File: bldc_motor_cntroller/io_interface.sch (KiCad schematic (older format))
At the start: 29 parts, among them J1 SM06B-SRSS-TB, J2 Conn_01x18, J5 0475900001, J6 TC2030 Tag-connect, J7 SH-SM02B-SRSS, SW1 SW_Push, SW2 SW_Push, U1 TCAN332GDCNT

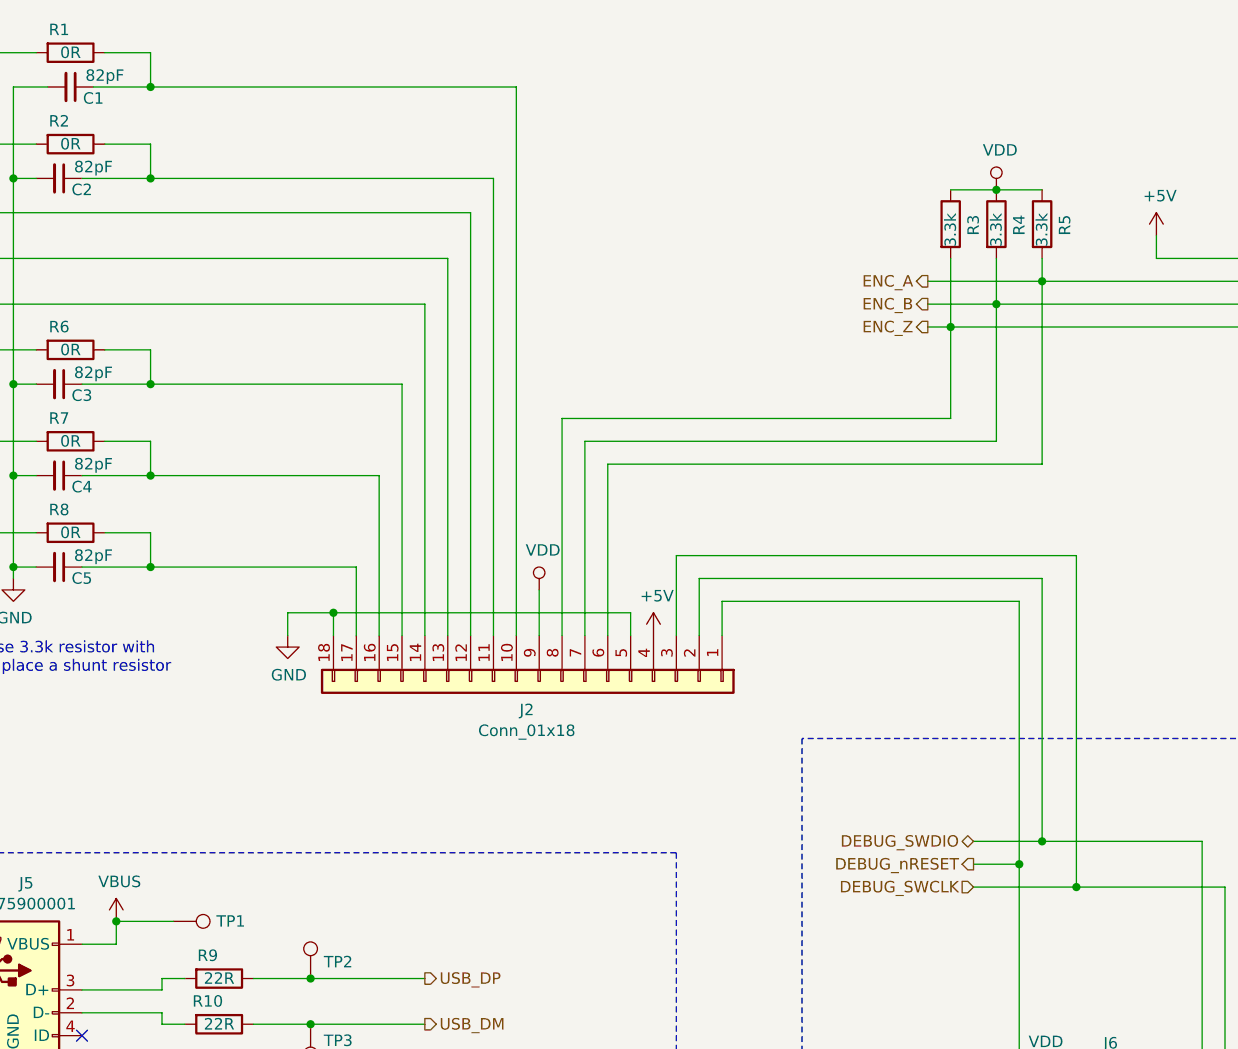
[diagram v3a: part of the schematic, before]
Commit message: swapped connections for better routing. highlighted serial gpios.
Signed-off-by: azmat bilal <azmat.bilal@outlook.com>
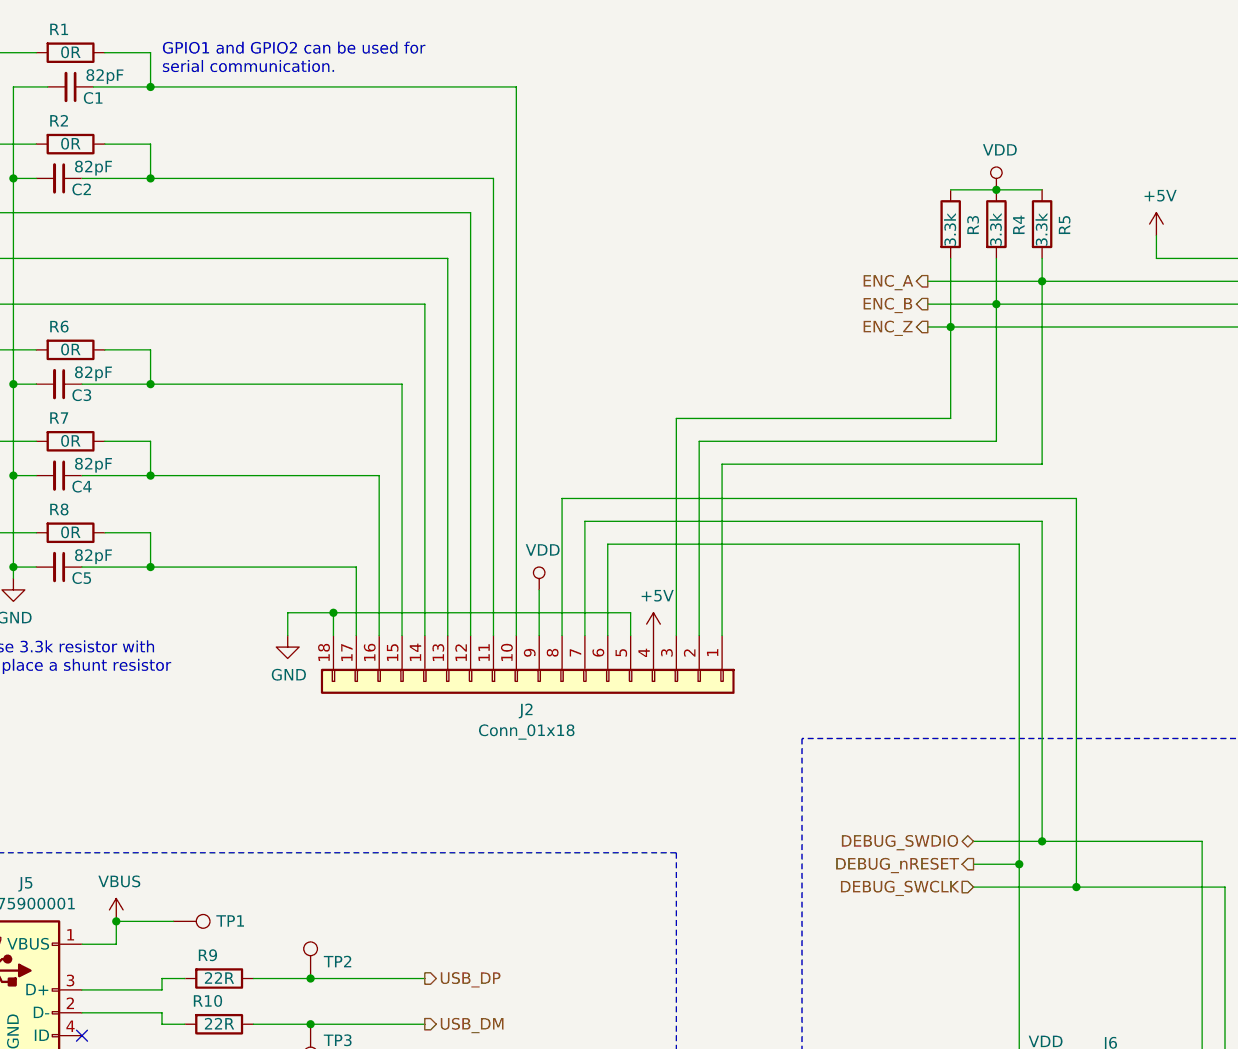
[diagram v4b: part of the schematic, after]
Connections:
- net DEBUG_SWCLK: now also J2.8 (Pin_8); no longer J2.3 (Pin_3)
- net DEBUG_SWDIO: now also J2.7 (Pin_7); no longer J2.2 (Pin_2)
- net DEBUG_nRESET: now also J2.6 (Pin_6); no longer J2.1 (Pin_1)
- net ENC_A: now also J2.1 (Pin_1); no longer J2.6 (Pin_6)
- net ENC_B: now also J2.2 (Pin_2); no longer J2.7 (Pin_7)
- net ENC_Z: now also J2.3 (Pin_3); no longer J2.8 (Pin_8)
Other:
- note added: "GPIO1 and GPIO2 can be used for\nserial communication."
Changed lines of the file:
@@
 	6300 2200 6300 2600
 Wire Wire Line
-	6300 2600 4600 2600
-Wire Wire Line
-	4600 2600 4600 3550
+	6300 2600 5100 2600
 Wire Wire Line
 	6500 2100 6500 2700
 Wire Wire Line
-	6500 2700 4700 2700
-Wire Wire Line
-	4700 2700 4700 3550
+	6500 2700 5200 2700
 Wire Wire Line
 	6700 2000 6700 2800
 Wire Wire Line
-	6700 2800 4800 2800
-Wire Wire Line
-	4800 2800 4800 3550
+	6700 2800 5300 2800
 $Comp
 L power:+5V #PWR?
@@
 Wire Wire Line
 	6600 5650 6750 5650
-Wire Wire Line
-	6600 4550 6600 3400
-Wire Wire Line
-	6600 3400 5300 3400
-Wire Wire Line
-	5300 3400 5300 3550
 Connection ~ 6600 4550
-Wire Wire Line
-	6700 4450 6700 3300
-Wire Wire Line
-	6700 3300 5200 3300
-Wire Wire Line
-	5200 3300 5200 3550
 Connection ~ 6700 4450
 Wire Wire Line
 	6700 4450 7400 4450
-Wire Wire Line
-	6850 4650 6850 3200
-Wire Wire Line
-	6850 3200 5100 3200
-Wire Wire Line
-	5100 3200 5100 3550
 Connection ~ 6850 4650
 Wire Wire Line
@@
 Wire Wire Line
 	4500 3350 4500 3550
+Wire Wire Line
+	6600 3150 4800 3150
+Wire Wire Line
+	4800 3150 4800 3550
+Wire Wire Line
+	6600 3150 6600 4550
+Wire Wire Line
+	6700 3050 4700 3050
+Wire Wire Line
+	4700 3050 4700 3550
+Wire Wire Line
+	6700 3050 6700 4450
+Wire Wire Line
+	6850 2950 4600 2950
+Wire Wire Line
+	4600 2950 4600 3550
+Wire Wire Line
+	6850 2950 6850 4650
+Wire Wire Line
+	5300 3550 5300 2800
+Wire Wire Line
+	5200 3550 5200 2700
+Wire Wire Line
+	5100 3550 5100 2600
+Text Notes 2850 1100 0    50   ~ 0
+GPIO1 and GPIO2 can be used for\nserial communication.
 $EndSCHEMATC

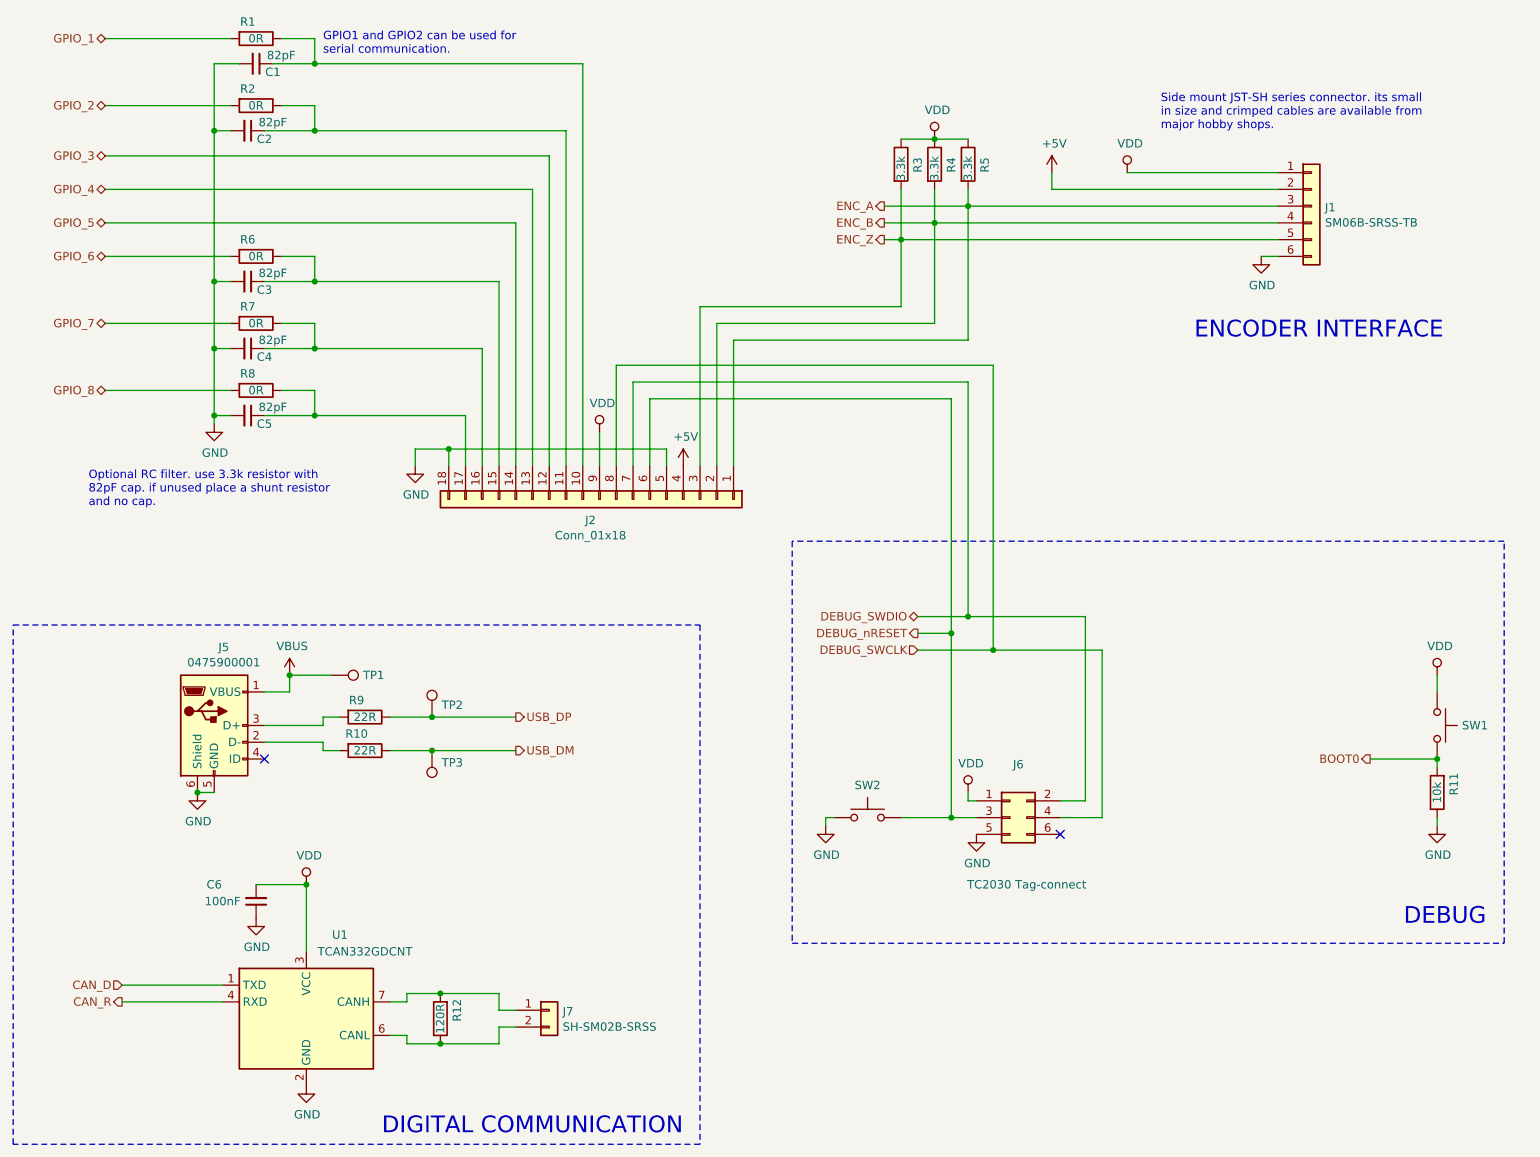
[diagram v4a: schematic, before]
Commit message: changed the SMD connector to JST SH (from JST SHL)
Signed-off-by: azmat bilal <azmat.bilal@outlook.com>
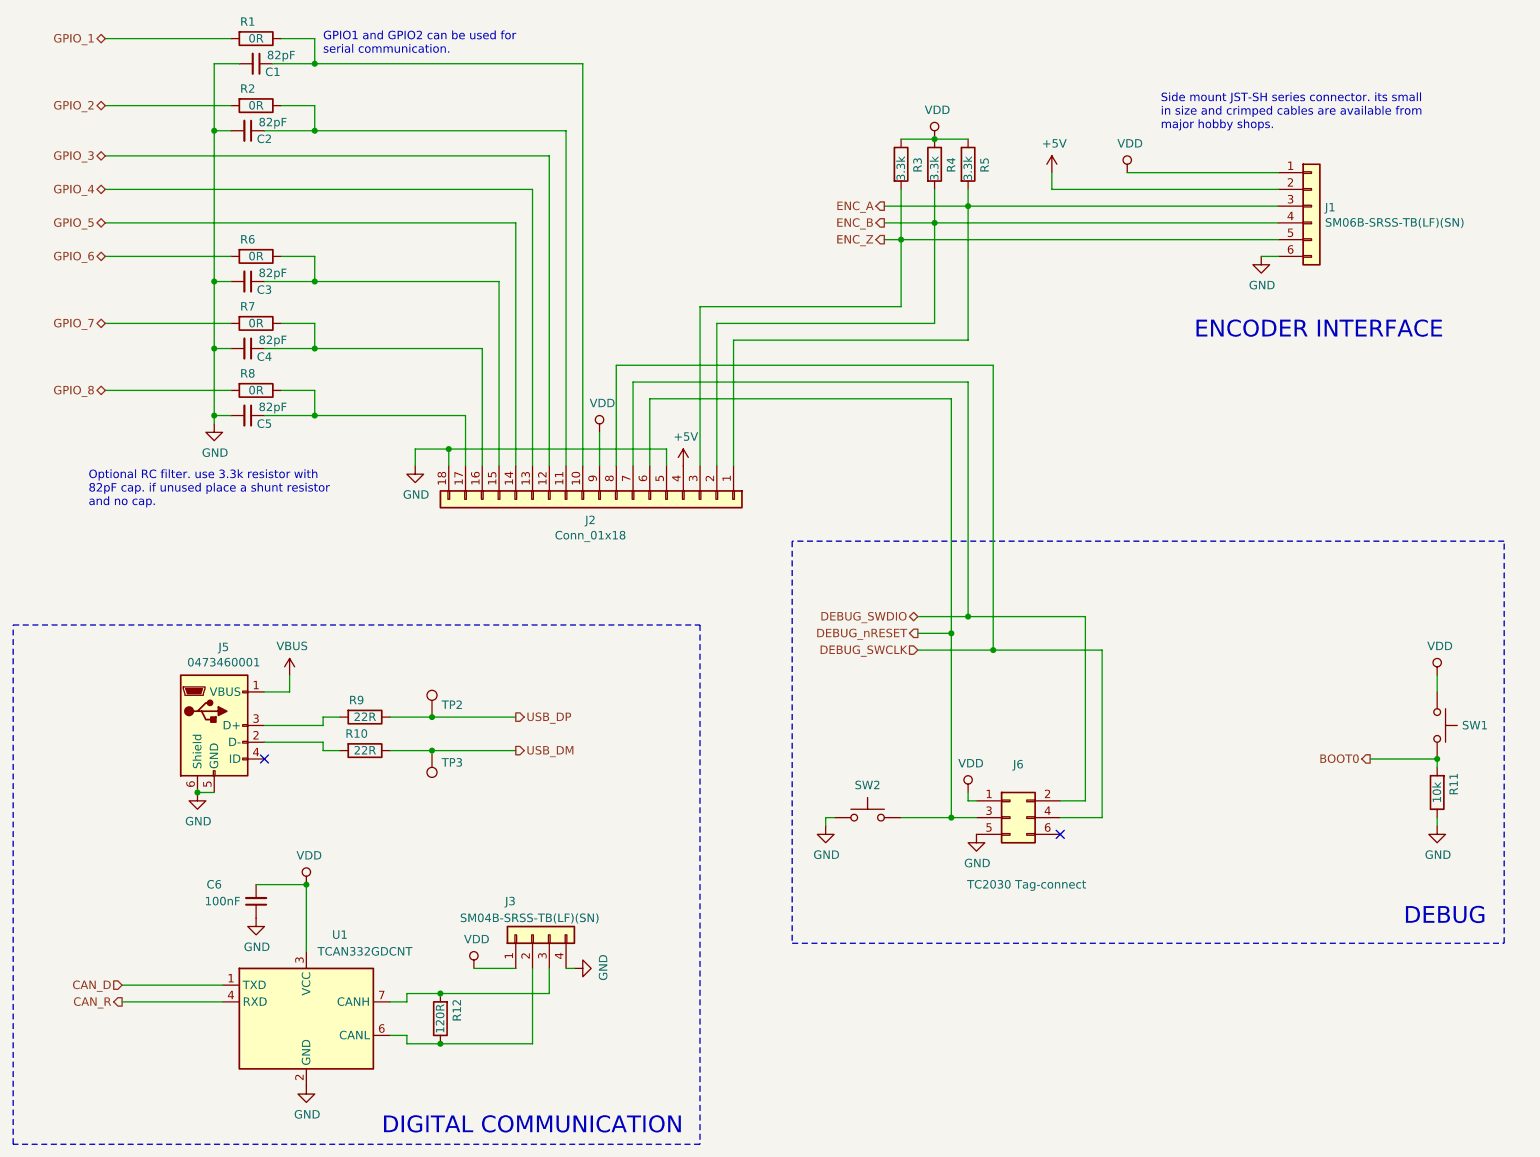
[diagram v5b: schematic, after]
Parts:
- removed J7: SH-SM02B-SRSS, Connector_JST:JST_SH_SM02B-SRSS-TB_1x02-1MP_P1.00mm_Horizontal, symbol Connector_Generic:Conn_01x02
- removed TP1: TestPoint, TestPoint:TestPoint_Pad_D1.5mm, symbol Connector:TestPoint
- added J3: SM04B-SRSS-TB(LF)(SN), Connector_JST:JST_SH_SM04B-SRSS-TB_1x04-1MP_P1.00mm_Horizontal, symbol Connector_Generic:Conn_01x04
- J1: value SM06B-SRSS-TB -> SM06B-SRSS-TB(LF)(SN)
- J5: value 0475900001 -> 0473460001; footprint Connector_USB:USB_Micro-AB_Molex_47590-0001 -> Connector_USB:USB_Micro-B_Molex_47346-0001
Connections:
- net GND: now also J3.4 (Pin_4)
- net VDD: now also J3.1 (Pin_1)
- net at R12.1, U1.6 (CANL): now also J3.2 (Pin_2)
- net at R12.2, U1.7 (CANH): now also J3.3 (Pin_3)
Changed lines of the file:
@@
 P 2200 5100
 F 0 "J5" H 2257 5567 50  0000 C CNN
-F 1 "0475900001" H 2257 5476 50  0000 C CNN
-F 2 "Connector_USB:USB_Micro-AB_Molex_47590-0001" H 2350 5050 50  0001 C CNN
+F 1 "0473460001" H 2257 5476 50  0000 C CNN
+F 2 "Connector_USB:USB_Micro-B_Molex_47346-0001" H 2350 5050 50  0001 C CNN
 F 3 "~" H 2350 5050 50  0001 C CNN
 	1    2200 5100
@@
 	2650 4900 2500 4900
 $Comp
-L Connector:TestPoint TP1
-U 1 1 5E39A600
-P 2900 4800
-F 0 "TP1" V 2900 4988 50  0000 L CNN
-F 1 "TestPoint" V 2945 4988 50  0001 L CNN
-F 2 "TestPoint:TestPoint_Pad_D1.5mm" H 3100 4800 50  0001 C CNN
-F 3 "~" H 3100 4800 50  0001 C CNN
-	1    2900 4800
-	0    1    1    0
-$EndComp
-Wire Wire Line
-	2900 4800 2650 4800
-Connection ~ 2650 4800
-$Comp
 L Connector:TestPoint TP2
 U 1 1 5E39DE72
@@
 Wire Wire Line
 	2750 6050 2750 6450
-$Comp
-L Connector_Generic:Conn_01x02 J7
-U 1 1 5E3CD122
-P 4200 6800
-F 0 "J7" H 4280 6792 50  0000 L CNN
-F 1 "SH-SM02B-SRSS" H 4280 6701 50  0000 L CNN
-F 2 "Connector_JST:JST_SH_SM02B-SRSS-TB_1x02-1MP_P1.00mm_Horizontal" H 4200 6800 50  0001 C CNN
-F 3 "~" H 4200 6800 50  0001 C CNN
-	1    4200 6800
-	1    0    0    -1
-$EndComp
-$Comp
-L Device:R R12
-U 1 1 5E3D290A
-P 3550 6850
-F 0 "R12" V 3450 6800 50  0000 C CNN
-F 1 "120R" V 3550 6850 50  0000 C CNN
-F 2 "Resistor_SMD:R_0402_1005Metric" V 3480 6850 50  0001 C CNN
-F 3 "~" H 3550 6850 50  0001 C CNN
-	1    3550 6850
-	-1   0    0    1
-$EndComp
 Wire Wire Line
 	3250 6750 3350 6750
@@
 	3350 6700 3550 6700
 Wire Wire Line
-	3900 6700 3900 6800
-Wire Wire Line
-	3900 6800 4000 6800
-Connection ~ 3550 6700
-Wire Wire Line
-	3550 6700 3900 6700
-Wire Wire Line
 	3250 6950 3350 6950
 Wire Wire Line
@@
 Wire Wire Line
 	3350 7000 3550 7000
-Wire Wire Line
-	3900 7000 3900 6900
-Wire Wire Line
-	3900 6900 4000 6900
-Connection ~ 3550 7000
-Wire Wire Line
-	3550 7000 3900 7000
 Text HLabel 1650 6650 0    50   Input ~ 0
 CAN_D
@@
 AR Path="/5E2D92A8/5E38F4AB" Ref="J1"  Part="1"
 F 0 "J1" H 8830 1992 50  0000 L CNN
-F 1 "SM06B-SRSS-TB" H 8830 1901 50  0000 L CNN
+F 1 "SM06B-SRSS-TB(LF)(SN)" H 8830 1901 50  0000 L CNN
 F 2 "Connector_JST:JST_SH_SM06B-SRSS-TB_1x06-1MP_P1.00mm_Horizontal" H 8750 2000 50  0001 C CNN
 F 3 "~" H 8750 2000 50  0001 C CNN
@@
 Text Notes 2850 1100 0    50   ~ 0
 GPIO1 and GPIO2 can be used for\nserial communication.
+$Comp
+L Connector_Generic:Conn_01x04 J3
+U 1 1 5E58BAE0
+P 4100 6350
+F 0 "J3" V 4300 6450 50  0000 L CNN
+F 1 "SM04B-SRSS-TB(LF)(SN)" V 4200 5950 50  0000 L CNN
+F 2 "Connector_JST:JST_SH_SM04B-SRSS-TB_1x04-1MP_P1.00mm_Horizontal" H 4100 6350 50  0001 C CNN
+F 3 "~" H 4100 6350 50  0001 C CNN
+	1    4100 6350
+	0    -1   -1   0
+$EndComp
+$Comp
+L power:VDD #PWR02
+U 1 1 5E58D69E
+P 3750 6550
+F 0 "#PWR02" H 3750 6400 50  0001 C CNN
+F 1 "VDD" H 3767 6723 50  0000 C CNN
+F 2 "" H 3750 6550 50  0001 C CNN
+F 3 "" H 3750 6550 50  0001 C CNN
+	1    3750 6550
+	1    0    0    -1
+$EndComp
+$Comp
+L power:GND #PWR03
+U 1 1 5E58D909
+P 4350 6550
+F 0 "#PWR03" H 4350 6300 50  0001 C CNN
+F 1 "GND" H 4355 6377 50  0000 C CNN
+F 2 "" H 4350 6550 50  0001 C CNN
+F 3 "" H 4350 6550 50  0001 C CNN
+	1    4350 6550
+	0    -1   -1   0
+$EndComp
+Wire Wire Line
+	4350 6550 4300 6550
+$Comp
+L Device:R R12
+U 1 1 5E3D290A
+P 3550 6850
+F 0 "R12" V 3450 6800 50  0000 C CNN
+F 1 "120R" V 3550 6850 50  0000 C CNN
+F 2 "Resistor_SMD:R_0402_1005Metric" V 3480 6850 50  0001 C CNN
+F 3 "~" H 3550 6850 50  0001 C CNN
+	1    3550 6850
+	-1   0    0    1
+$EndComp
+Wire Wire Line
+	3550 6700 4200 6700
+Wire Wire Line
+	4200 6700 4200 6550
+Connection ~ 3550 6700
+Wire Wire Line
+	4100 6550 4100 7000
+Wire Wire Line
+	4100 7000 3550 7000
+Connection ~ 3550 7000
+Wire Wire Line
+	3750 6550 4000 6550
 $EndSCHEMATC

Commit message: improved assembly documentation
Signed-off-by: azmat bilal <azmat.bilal@outlook.com>
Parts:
- SW1, SW2: value SW_Push -> B3U-1000P-B
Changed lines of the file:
@@
 P 6100 5650
 F 0 "SW2" H 6100 5843 50  0000 C CNN
-F 1 "SW_Push" H 6100 5844 50  0001 C CNN
+F 1 "B3U-1000P-B" H 6100 5844 50  0001 C CNN
 F 2 "Button_Switch_SMD:SW_SPST_B3U-1000P" H 6100 5850 50  0001 C CNN
 F 3 "~" H 6100 5850 50  0001 C CNN
@@
 P 9500 5100
 F 0 "SW1" V 9500 5248 50  0000 L CNN
-F 1 "SW_Push" H 9500 5294 50  0001 C CNN
+F 1 "B3U-1000P-B" H 9500 5294 50  0001 C CNN
 F 2 "Button_Switch_SMD:SW_SPST_B3U-1000P" H 9500 5300 50  0001 C CNN
 F 3 "~" H 9500 5300 50  0001 C CNN
